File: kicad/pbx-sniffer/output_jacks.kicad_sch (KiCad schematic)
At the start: 24 parts

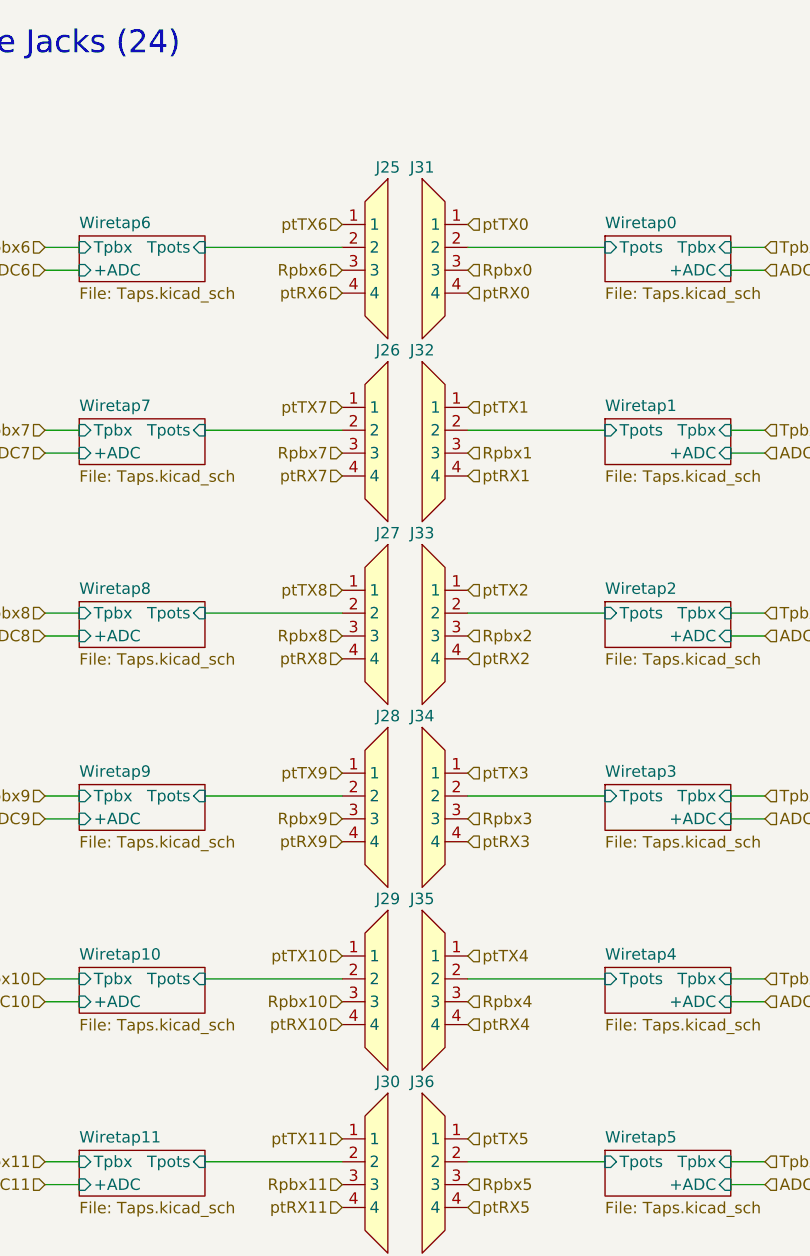
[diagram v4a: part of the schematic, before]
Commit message: initial module structure, for tiling later
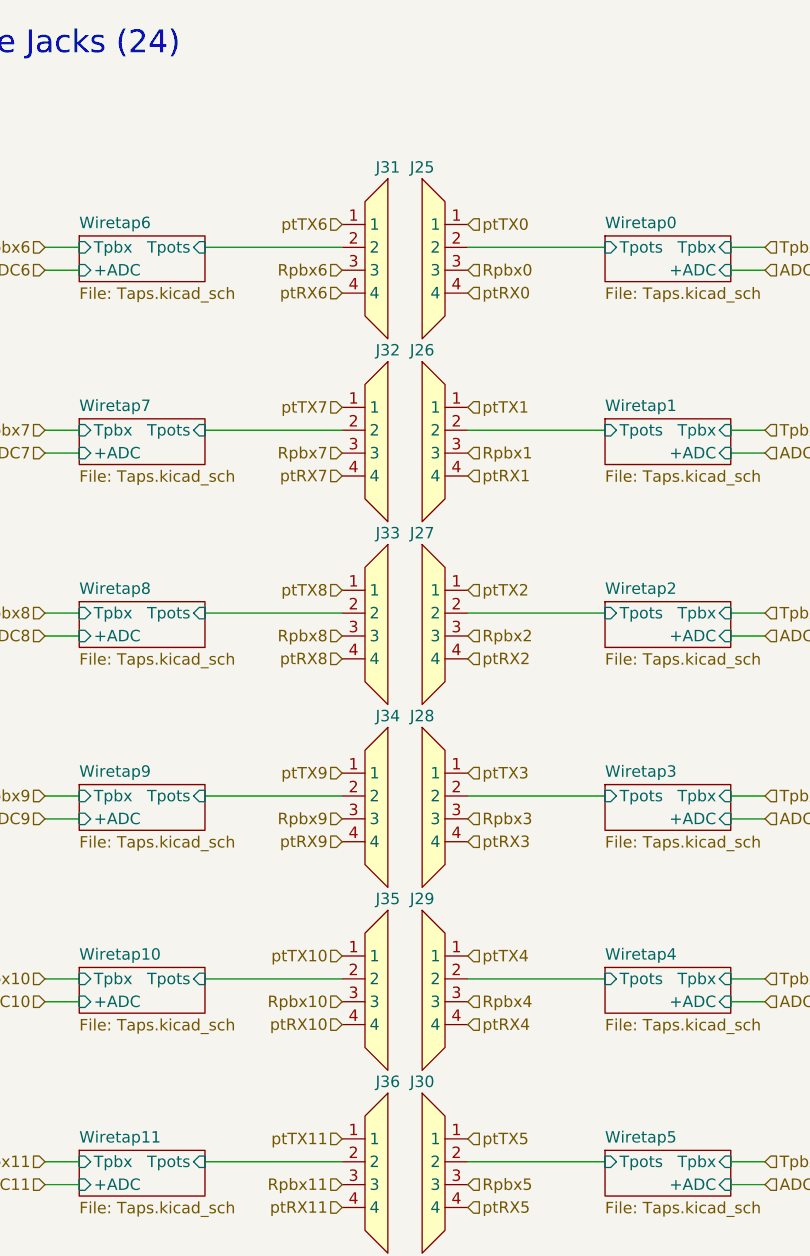
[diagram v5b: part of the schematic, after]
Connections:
- net Rpbx0: now also J25.3; no longer J31.3
- net Rpbx1: now also J26.3; no longer J32.3
- net Rpbx10: now also J35.3; no longer J29.3
- net Rpbx11: now also J36.3; no longer J30.3
- net Rpbx2: now also J27.3; no longer J33.3
- net Rpbx3: now also J28.3; no longer J34.3
- net Rpbx4: now also J29.3; no longer J35.3
- net Rpbx5: now also J30.3; no longer J36.3
- net Rpbx6: now also J31.3; no longer J25.3
- net Rpbx7: now also J32.3; no longer J26.3
- net Rpbx8: now also J33.3; no longer J27.3
- net Rpbx9: now also J34.3; no longer J28.3
- net Wiretap0/Tpots: now also J25.2; no longer J31.2
- net Wiretap1/Tpots: now also J26.2; no longer J32.2
- net Wiretap10/Tpots: now also J35.2; no longer J29.2
- net Wiretap11/Tpots: now also J36.2; no longer J30.2
- net Wiretap2/Tpots: now also J27.2; no longer J33.2
- net Wiretap3/Tpots: now also J28.2; no longer J34.2
- net Wiretap4/Tpots: now also J29.2; no longer J35.2
- net Wiretap5/Tpots: now also J30.2; no longer J36.2
- net Wiretap6/Tpots: now also J31.2; no longer J25.2
- net Wiretap7/Tpots: now also J32.2; no longer J26.2
- net Wiretap8/Tpots: now also J33.2; no longer J27.2
- net Wiretap9/Tpots: now also J34.2; no longer J28.2
- net ptRX0: now also J25.4; no longer J31.4
- net ptRX1: now also J26.4; no longer J32.4
- net ptRX10: now also J35.4; no longer J29.4
- net ptRX11: now also J36.4; no longer J30.4
- net ptRX2: now also J27.4; no longer J33.4
- net ptRX3: now also J28.4; no longer J34.4
- net ptRX4: now also J29.4; no longer J35.4
- net ptRX5: now also J30.4; no longer J36.4
- net ptRX6: now also J31.4; no longer J25.4
- net ptRX7: now also J32.4; no longer J26.4
- net ptRX8: now also J33.4; no longer J27.4
- net ptRX9: now also J34.4; no longer J28.4
- net ptTX0: now also J25.1; no longer J31.1
- net ptTX1: now also J26.1; no longer J32.1
- net ptTX10: now also J35.1; no longer J29.1
- net ptTX11: now also J36.1; no longer J30.1
- net ptTX2: now also J27.1; no longer J33.1
- net ptTX3: now also J28.1; no longer J34.1
- net ptTX4: now also J29.1; no longer J35.1
- net ptTX5: now also J30.1; no longer J36.1
- net ptTX6: now also J31.1; no longer J25.1
- net ptTX7: now also J32.1; no longer J26.1
- net ptTX8: now also J33.1; no longer J27.1
- net ptTX9: now also J34.1; no longer J28.1
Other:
- moved on the sheet: J25, J26, J27, J28, J29, J30, J31, J32, J33, J34, J35, J36

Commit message: update to kicad 10 & fix nucleo symbol to use background color
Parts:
- J25, J26, J27, J28, J29, J30, J31, J32, J33, J34, J35, J36, J37, J38, J39, J40, J41, J42, J43, J44, J45, J46, J47, J48: value ~ -> (none)
